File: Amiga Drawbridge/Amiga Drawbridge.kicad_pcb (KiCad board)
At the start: 2 copper layers, 90 x 94 mm, 18 parts, among them J1 FDC, J2 PWR_EXT1, J3 PWR_DRV, J4 PWR_EXT2, M1 Mounting, M2 Mounting, M3 Mounting, M4 Mounting

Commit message: Export files
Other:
- board text added: "LOFOTEN"
- board text removed: "MADE IN LOFOTEN"

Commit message: Changed made by notice
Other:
- board text added: "DESIGNED IN LOFOTEN"
- board text removed: "LOFOTEN"

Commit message: Fix silkscreen error
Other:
- board text added: "PWR_SEL: 1-2 5v barrel jack 2-3 USB"
- board text removed: "PWR_SEL: 1-2 USB 2-3 5v barrel jack"

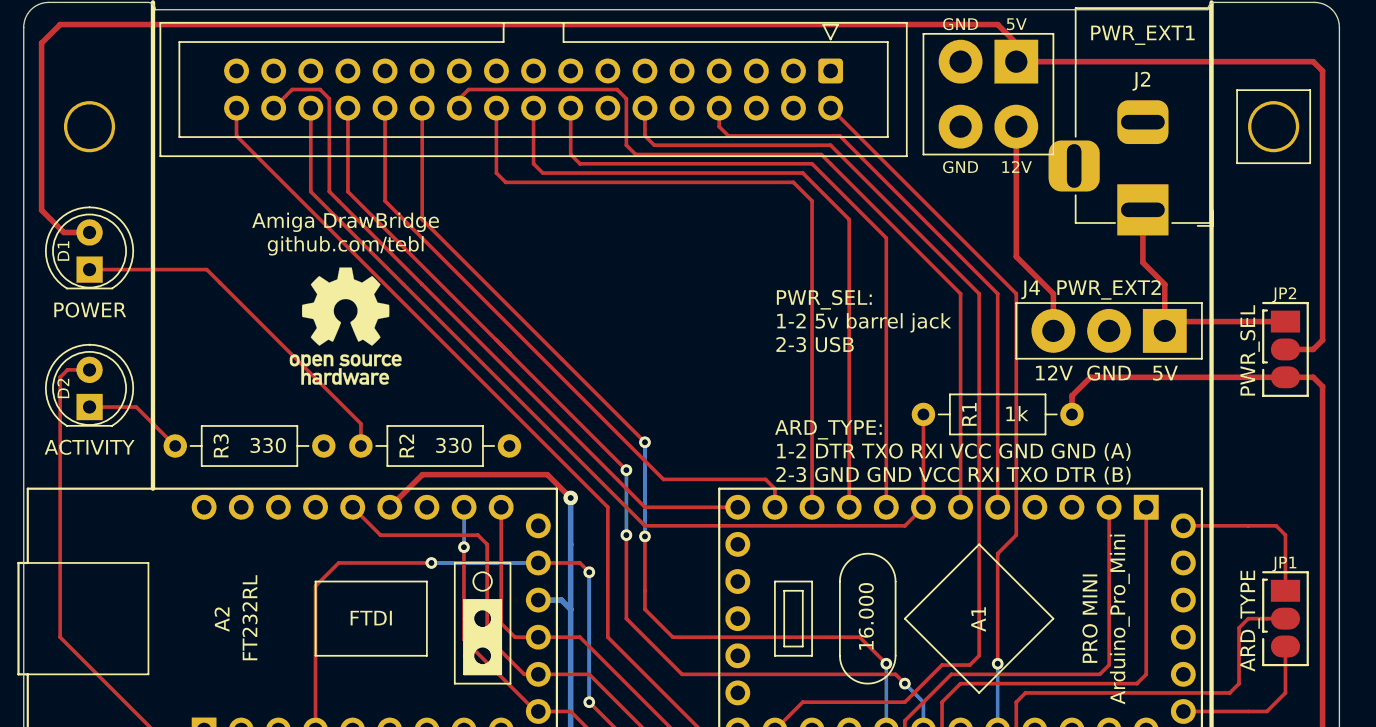
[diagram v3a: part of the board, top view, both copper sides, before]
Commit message: Can swap D4 and D8
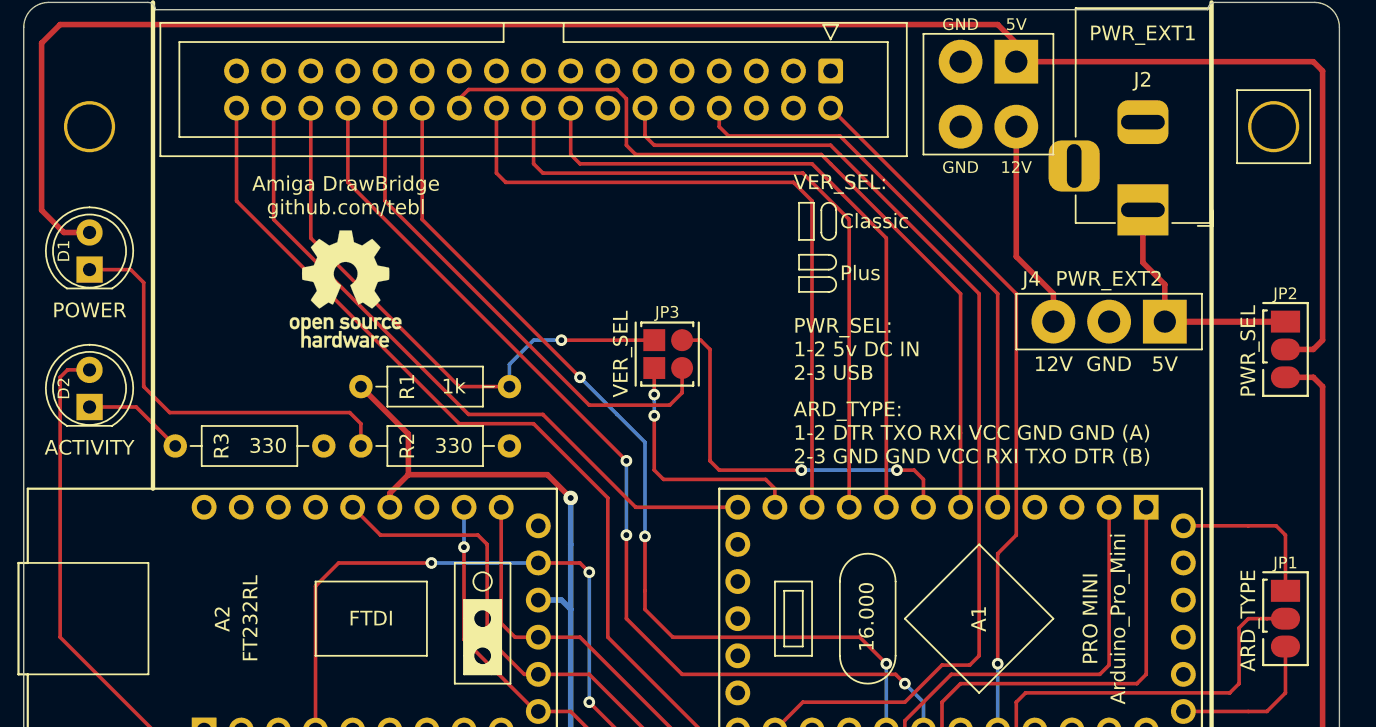
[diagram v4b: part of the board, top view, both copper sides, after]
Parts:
- added JP3: VER_SEL, solder_bridge:select_swappable, F.Cu at (151.1, 78.1)
- moved R1 38.5 mm to (141.2, 81.3)
- moved REF** 2.54 mm to (130.0, 74.6)
- moved J4 0.63 mm to (182.2, 80.0)
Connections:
- A1 pad 11: /~TRK00 -> Net-(A1-Pad11)
- A1 pad 7: /~RDATA -> Net-(A1-Pad7)
- R1 pad 1: VCC -> /~RDATA
- R1 pad 2: /~RDATA -> VCC
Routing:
- net Net-(A1-Pad7): track 0.00 -> 26.8 mm, vias 0 -> 2
- net /~RDATA: track 64.0 -> 38.5 mm, vias 0 -> 1
- net Net-(A1-Pad11): track 0.00 -> 17.0 mm, vias 0 -> 2
- net VCC: track 132.5 -> 124.0 mm
- net Net-(J2-Pad1): track 17.4 -> 25.7 mm
- net /~TRK00: track 42.4 -> 34.5 mm
- net Net-(D1-Pad1): track 24.5 -> 28.6 mm
- net /~DSKCHG: track 58.2 -> 61.2 mm
- net /~WPT: track 68.8 -> 67.4 mm
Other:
- board text added: "Classic"
- board text added: "PWR_SEL: 1-2 5v DC IN 2-3 USB"
- board text added: "Plus"
- board text added: "VER_SEL:"
- board text removed: "PWR_SEL: 1-2 5v barrel jack 2-3 USB"
